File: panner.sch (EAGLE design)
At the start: 49 parts, among them U1 MAX5419LETA+, U2 MAX5419LETA+, X1 OPAMP, X10 OPAMP, X3 OPAMP, X5 OPAMP, X6 OPAMP, X7 OPAMP, X8 OPAMP, X9 OPAMP

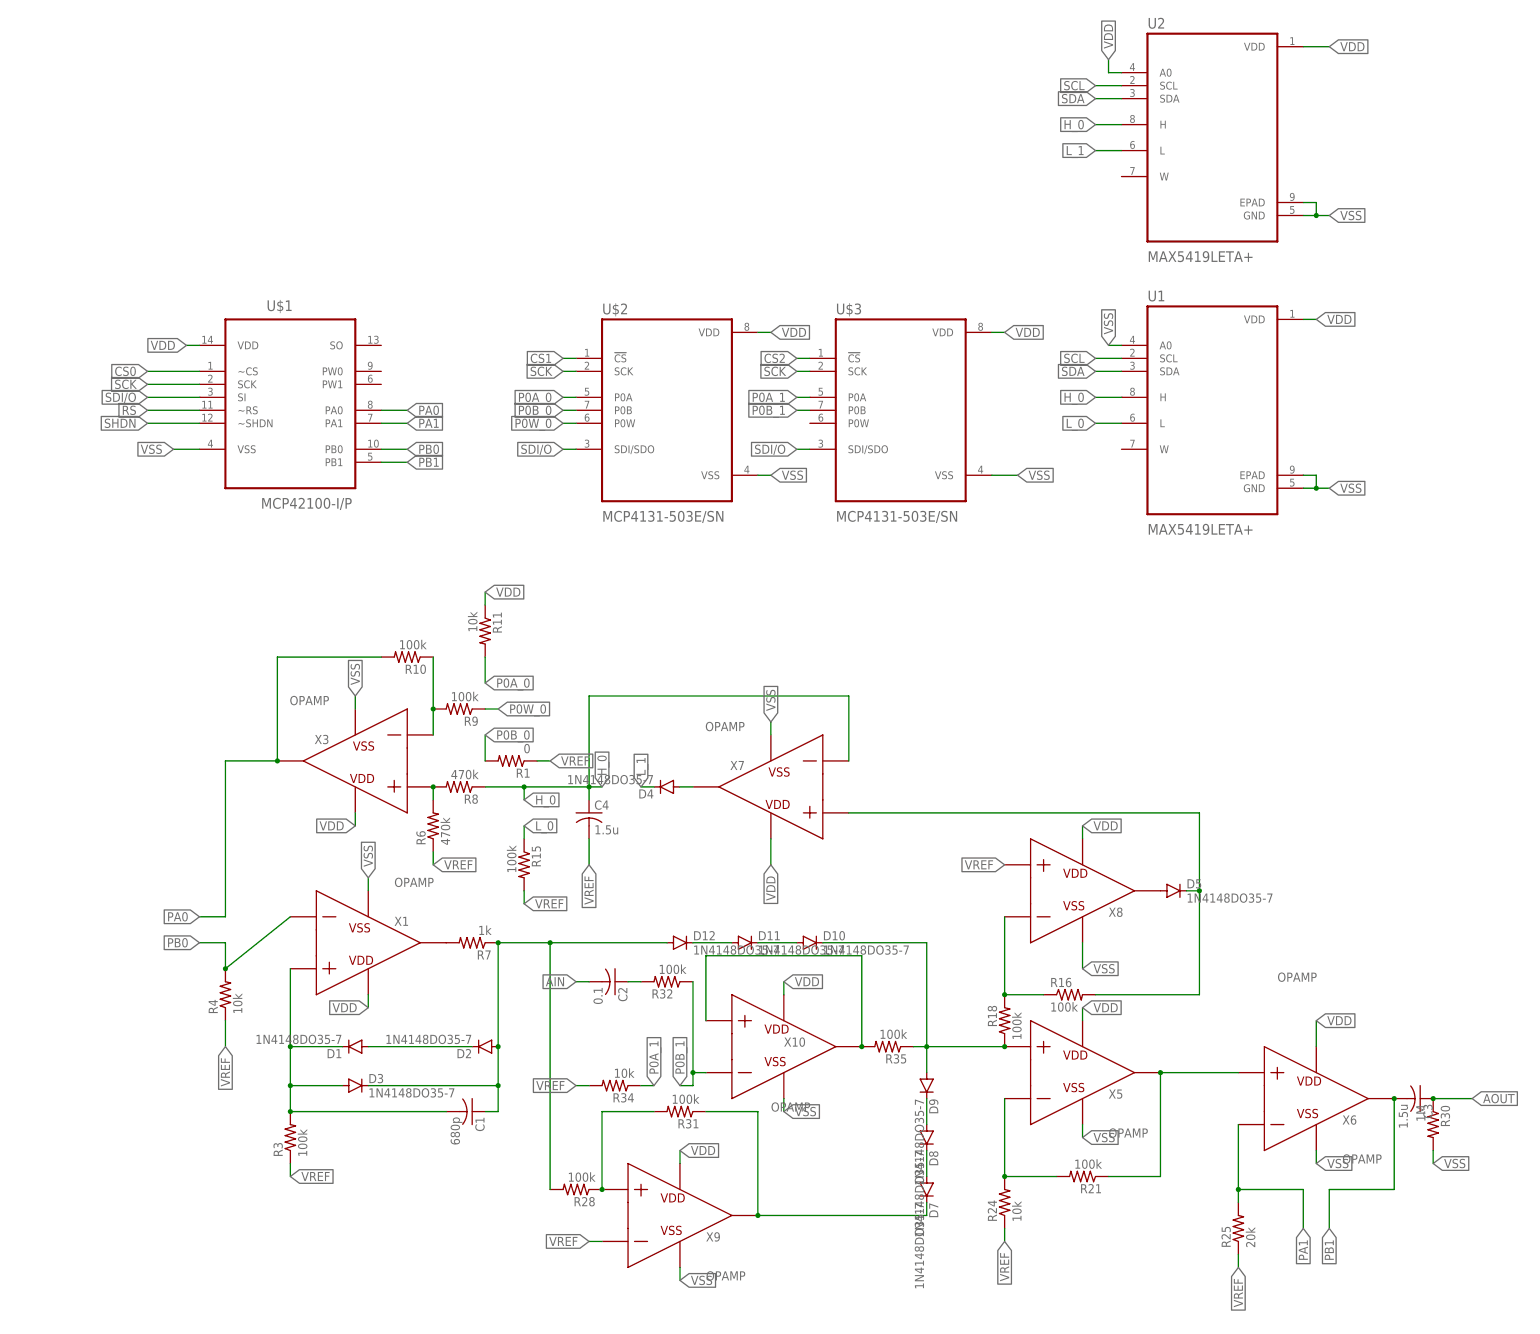
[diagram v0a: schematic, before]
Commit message: update, split out into schematics for each component
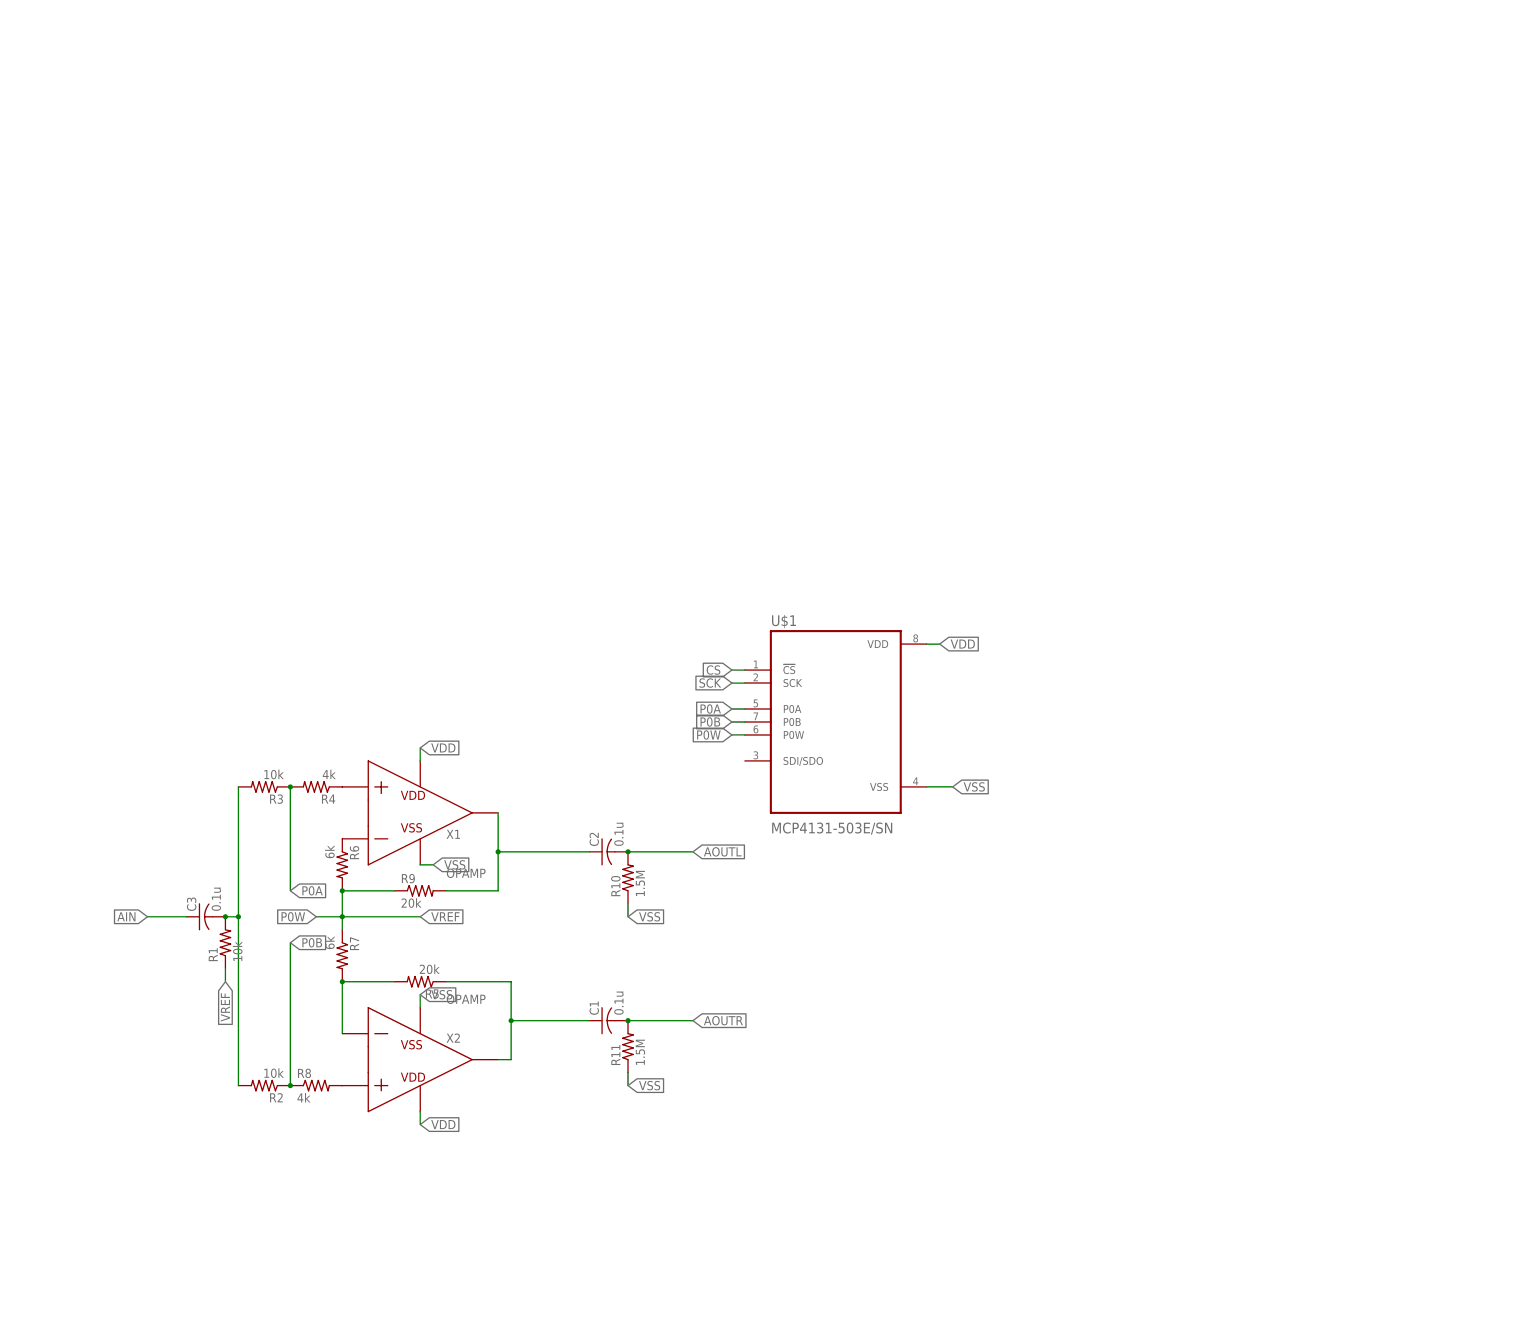
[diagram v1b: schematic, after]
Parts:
- removed C4: 1.5u, rcl:C-US025-024X044
- removed D1, D10, D11, D12, D2, D3, D4, D5, D7, D8, D9: 1N4148DO35-7, diode:1N4148DO35-7
- removed R15, R16, R18, R21, R28, R31, R32, R35: 100k, rcl:R-US_0204/7
- removed R24, R34: 10k, rcl:R-US_0204/7
- removed R25: 20k, rcl:R-US_0204/7
- removed R30: 1M, rcl:R-US_0204/7
- removed U$2, U$3: MCP4131-503E/SN, MCP4131-503E_SN:MCP4131-503E/SN
- removed U1, U2: MAX5419LETA+, MAX5419LETA_:MAX5419LETA+
- removed X10, X3, X5, X6, X7, X8, X9: OPAMP, ngspice-simulation:OPAMP
- added R2: 10k, rcl:R-US_0204/5
- added R5: 20k, rcl:R-US_0204/5
- added X2: OPAMP, ngspice-simulation:OPAMP
- C1: value 680p -> 0.1u
- C2: value 0.1 -> 0.1u
- C3: value 1.5u -> 0.1u
- R1: value 0 -> 10k; device rcl:R-US_0204/7 -> rcl:R-US_0204/5
- R10: value 100k -> 1.5M; device rcl:R-US_0204/7 -> rcl:R-US_0204/5
- R11: value 10k -> 1.5M; device rcl:R-US_0204/7 -> rcl:R-US_0204/5
- R3: value 100k -> 10k; device rcl:R-US_0204/7 -> rcl:R-US_0204/5
- R4: value 10k -> 4k; device rcl:R-US_0204/7 -> rcl:R-US_0204/5
- R6: value 470k -> 6k; device rcl:R-US_0204/7 -> rcl:R-US_0204/5
- R7: value 1k -> 6k; device rcl:R-US_0204/7 -> rcl:R-US_0204/5
- R8: value 470k -> 4k; device rcl:R-US_0204/7 -> rcl:R-US_0204/5
- R9: value 100k -> 20k; device rcl:R-US_0204/7 -> rcl:R-US_0204/5
- U$1: value MCP42100-I/P -> MCP4131-503E/SN; device MCP42100-I_P:MCP42100-I/P -> MCP4131-503E_SN:MCP4131-503E/SN; SPICEPREFIX (none) -> X
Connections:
- removed net AOUT: C3.1, R30.1
- removed net CS0: U$1.~CS
- removed net CS1: U$2.!CS
- removed net CS2: U$3.!CS
- removed net H_0: C4.1, R8.1, U1.H, U2.H, X7.N
- removed net L_0: R15.1, U1.L
- removed net L_1: D4.C, U2.L
- removed net N$1: R7.2, X1.VOUT
- removed net N$14: D4.A, X7.VOUT
- removed net N$15: D5.C, R16.2, X7.P
- removed net N$16: R16.1, R18.2, X8.N
- removed net N$18: R21.1, X5.VOUT, X6.P
- removed net N$19: R21.2, R24.2, X5.N
- removed net N$20: D1.A, D2.C
- removed net N$21: C1.1, D12.A, D2.A, D3.C, R28.2, R7.1
- removed net N$22: R28.1, R31.2, X9.P
- removed net N$23: D7.C, R31.1, X9.VOUT
- removed net N$24: D8.A, D9.C
- removed net N$25: D7.A, D8.C
- removed net N$26: D10.C, D9.A, R18.1, R35.1, X5.P
- removed net N$27: R35.2, X10.P, X10.VOUT
- removed net N$3: C1.2, D1.C, D3.A, R3.2, X1.P
- removed net N$30: C2.1, R32.2
- removed net N$31: D11.A, D12.C
- removed net N$32: D10.A, D11.C
- removed net N$33: D5.A, X8.VOUT
- removed net P0A_0: R11.2, U$2.P0A
- removed net P0A_1: R34.1, U$3.P0A
- removed net P0B_0: R1.2, U$2.P0B
- removed net P0B_1: R32.1, U$3.P0B, X10.N
- removed net P0W_0: R9.1, U$2.P0W
- removed net PA0: R10.2, U$1.PA0, X3.VOUT
- removed net PA1: R25.2, U$1.PA1, X6.N
- removed net PB0: R4.2, U$1.PB0, X1.N
- removed net PB1: C3.2, U$1.PB1, X6.VOUT
- removed net RS: U$1.~RS
- removed net SCL: U1.SCL, U2.SCL
- removed net SDA: U1.SDA, U2.SDA
- removed net SDI/O: U$1.SI, U$2.SDI/SDO, U$3.SDI/SDO
- removed net SHDN: U$1.~SHDN
- new net AOUTL: C2.2, R10.2
- new net AOUTR: C1.2, R11.2
- new net CS: U$1.!CS
- new net N$12: R8.2, X2.P
- new net N$13: R4.1, X1.P
- new net N$2: C3.2, R1.2, R2.2, R3.2
- new net N$8: C1.1, R5.1, X2.VOUT
- new net N$9: C2.1, R9.2, X1.VOUT
- new net P0A: R3.1, R4.2, U$1.P0A
- new net P0B: R2.1, R8.1, U$1.P0B
- new net P0W: R6.2, R7.1, R9.1, U$1.P0W
- net AIN: now also C3.1; no longer C2.2
- net N$6: now also R6.1, X1.N; no longer R6.2, R8.2, X3.P
- net N$7: now also R5.2, R7.2, X2.N; no longer R10.1, R9.2, X3.N
- net SCK: no longer U$2.SCK, U$3.SCK
- net VDD: now also X2.VDD; no longer R11.1, U$2.VDD, U$3.VDD, U1.VDD, U2.A0, U2.VDD, X10.VDD, X3.VDD, X5.VDD, X6.VDD, X7.VDD, X8.VDD, X9.VDD
- net VREF: no longer C4.2, R15.2, R24.1, R25.1, R3.1, R34.2, R4.1, R6.1, X9.N
- net VSS: now also R10.1, R11.1, X2.VSS; no longer R30.2, U$2.VSS, U$3.VSS, U1.A0, U1.EPAD, U1.GND, U2.EPAD, U2.GND, X10.VSS, X3.VSS, X5.VSS, X6.VSS, X7.VSS, X8.VSS, X9.VSS
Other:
- moved on the sheet: C1, C2, C3, R1, R10, R11, R3, R4, R6, R7, R8, R9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

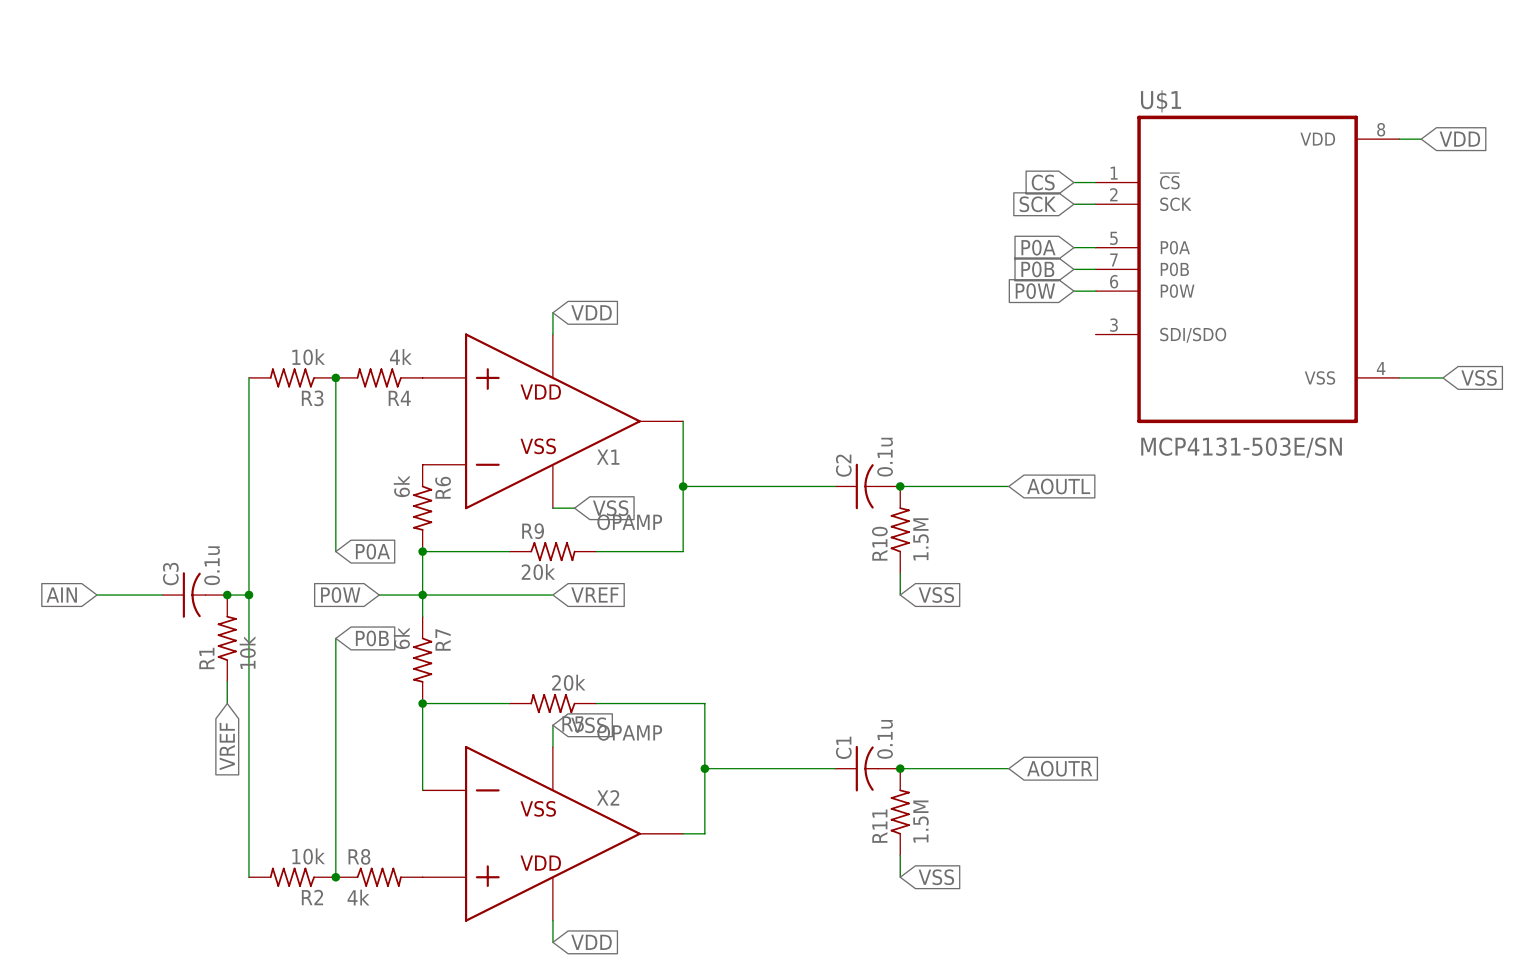
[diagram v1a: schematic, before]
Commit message: rm cache files, add boards for components
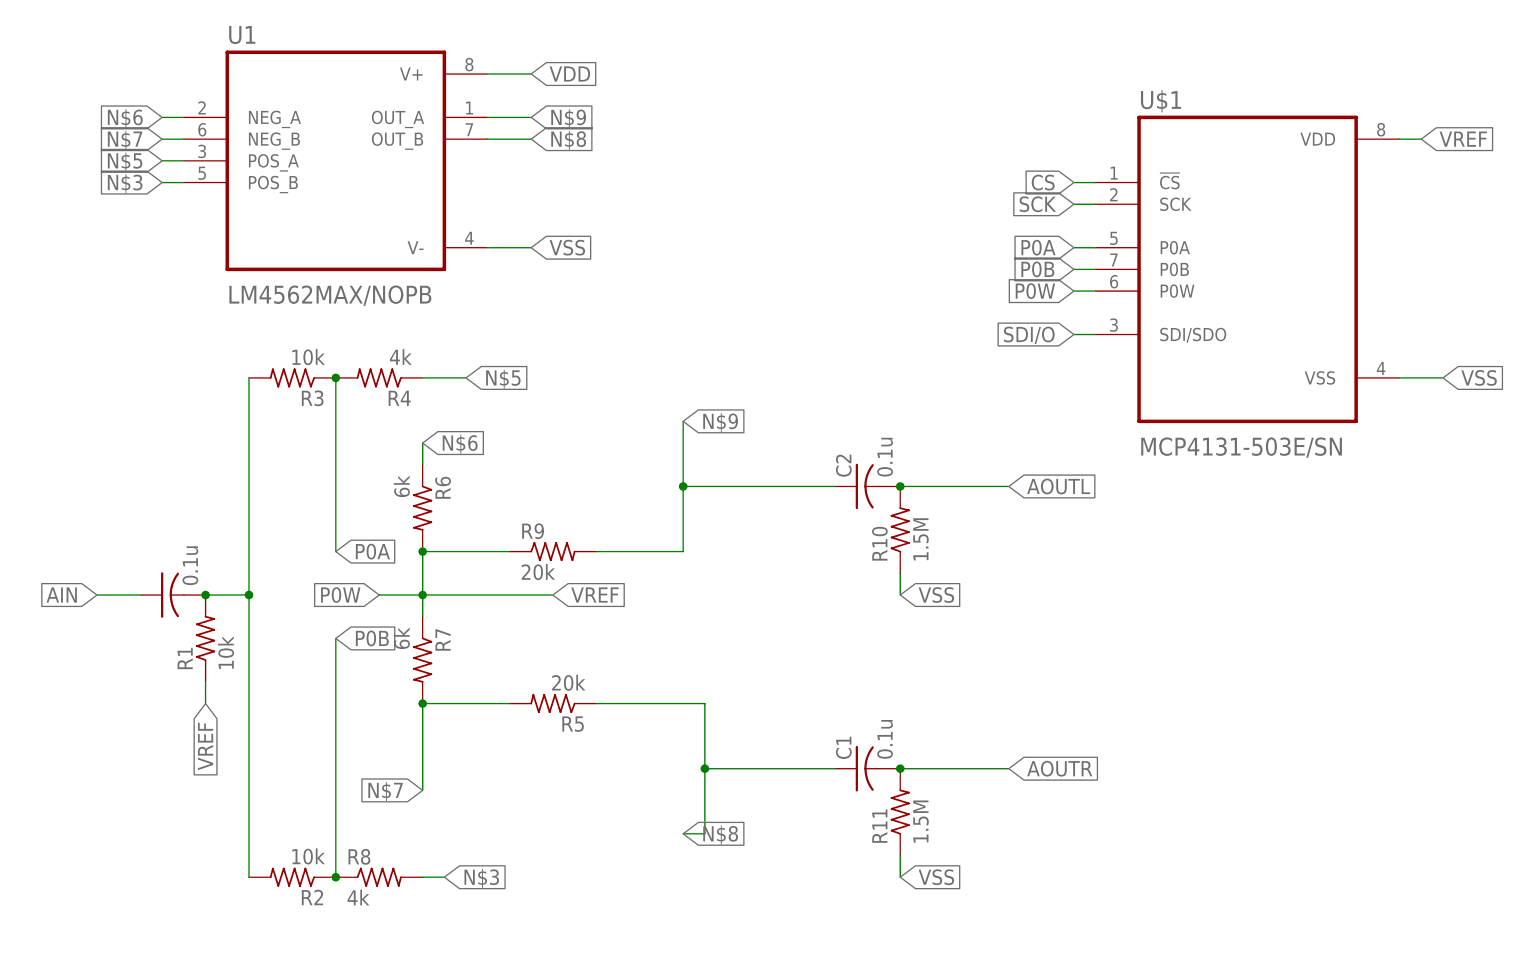
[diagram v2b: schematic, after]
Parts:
- removed X1, X2: OPAMP, ngspice-simulation:OPAMP
- added U1: LM4562MAX/NOPB, LM4562MAX_NOPB:LM4562MAX/NOPB
- C1, C2, C3: device rcl:C-US025-024X044 -> rcl:C-USC0402
- R1, R10, R11, R2, R3, R4, R5, R6, R7, R8, R9: device rcl:R-US_0204/5 -> rcl:R-US_R0402
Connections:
- removed net N$12: R8.2, X2.P
- removed net N$13: R4.1, X1.P
- new net N$3: R8.2, U1.POS_B
- new net N$5: R4.1, U1.POS_A
- new net SDI/O: U$1.SDI/SDO
- net N$6: now also U1.NEG_A; no longer X1.N
- net N$7: now also U1.NEG_B; no longer X2.N
- net N$8: now also U1.OUT_B; no longer X2.VOUT
- net N$9: now also U1.OUT_A; no longer X1.VOUT
- net VDD: now also U1.V+; no longer U$1.VDD, X1.VDD, X2.VDD
- net VREF: now also U$1.VDD
- net VSS: now also U1.V-; no longer X1.VSS, X2.VSS
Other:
- moved on the sheet: R1

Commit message: corrections
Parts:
- removed C1, C2, C3: 0.1u, rcl:C-USC0402
- removed R10, R11: 1.5M, rcl:R-US_R0402
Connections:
- removed net N$2: C3.2, R1.2, R2.2, R3.2
- removed net N$8: C1.1, R5.1, U1.OUT_B
- removed net N$9: C2.1, R9.2, U1.OUT_A
- removed net P0W: R6.2, R7.1, R9.1, U$1.P0W
- removed net VSS: R10.1, R11.1, U$1.VSS, U1.V-
- new net GND: U$1.VSS, U1.V-
- net AIN: now also R1.2, R2.2, R3.2; no longer C3.1
- net AOUTL: now also R9.2, U1.OUT_A; no longer C2.2, R10.2
- net AOUTR: now also R5.1, U1.OUT_B; no longer C1.2, R11.2
- net N$6: now also R9.1
- net VREF: now also R6.2, R7.1, U$1.P0W
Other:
- moved on the sheet: R6, R9, U$1

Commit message: updates
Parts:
- removed R6, R7: 6k, rcl:R-US_R0402
- removed U$1: MCP4131-503E/SN, MCP4131-503E_SN:MCP4131-503E/SN
- added 10KPOT1_PAN: MCP4131-503E/SN, MCP4131-503E_SN:MCP4131-503E/SN
- added C1: 10uF, rcl:C-USC0402
- added D1: 1N4148W-TPSOD123-L, 1N4148W-TP:1N4148W-TPSOD123-L
- R1: value 10k -> 1M
- R2, R3: value 10k -> 5k
- R4, R8: value 4k -> 5k
- R5, R9: value 20k -> 10k
- renumbered U1 to OPAMP1_PAN
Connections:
- net AOUTL renamed OUTL_PAN
- net AOUTR renamed OUTR_PAN
- removed net AIN: R1.2, R2.2, R3.2
- removed net CS: U$1.!CS
- removed net N$3: OPAMP1_PAN.POS_B, R8.2
- removed net N$5: OPAMP1_PAN.POS_A, R4.1
- removed net N$6: OPAMP1_PAN.NEG_A, R6.1, R9.1
- removed net N$7: OPAMP1_PAN.NEG_B, R5.2, R7.2
- removed net P0A: R3.1, R4.2, U$1.P0A
- removed net P0B: R2.1, R8.1, U$1.P0B
- new net CS_PAN: 10KPOT1_PAN.!CS
- new net IN_PAN: C1.1
- new net N$1: C1.2, R1.2, R2.2, R3.2
- new net NEG_A_PAN: OPAMP1_PAN.NEG_A, R4.1, R9.1
- new net NEG_B_PAN: OPAMP1_PAN.NEG_B, R5.2, R8.2
- new net P0A_PAN: 10KPOT1_PAN.P0A, R3.1, R4.2
- new net P0B_PAN: 10KPOT1_PAN.P0B, R2.1, R8.1
- new net P0W_PAN: 10KPOT1_PAN.P0W, D1.C
- net GND: now also 10KPOT1_PAN.VSS; no longer U$1.VSS
- net SCK: now also 10KPOT1_PAN.SCK; no longer U$1.SCK
- net SDI/O: now also 10KPOT1_PAN.SDI/SDO; no longer U$1.SDI/SDO
- net VREF: now also 10KPOT1_PAN.VDD, D1.A, OPAMP1_PAN.POS_A, OPAMP1_PAN.POS_B; no longer R6.2, R7.1, U$1.P0W, U$1.VDD
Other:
- moved on the sheet: R1, R2, R3, R5, R8, R9
